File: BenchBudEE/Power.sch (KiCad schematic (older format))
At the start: 0 parts

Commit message: Power Protection and filtering module added
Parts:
- added C? (x2): C, ~, symbol C
- added F? (x4): FUSE, ~, symbol FUSE
- added L? (x2): INDUCTOR, ~, symbol INDUCTOR
- added P?: CONN_12X2, symbol CONN_12X2
- added R?: R, ~, symbol R
- added SW?: SWITCH_INV, ~, symbol SWITCH_INV
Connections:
- net labels added: +12P, +12V, +3.3V, +5V, -12P, -12V, GND
- wire segments 0 -> 39

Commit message: Fan/current module refactoring
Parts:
- removed F? (x4): FUSE, ~, symbol FUSE
- added TH? (x4): THERMISTOR, ~, symbol THERMISTOR
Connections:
- net labels added: +12C
- wire segments 39 -> 40
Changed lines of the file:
@@
 $Descr A4 11693 8268
 encoding utf-8
-Sheet 6 9
+Sheet 4 9
 Title ""
-Date "9 feb 2014"
+Date "11 feb 2014"
 Rev ""
 Comp ""
@@
 F 3 "" H 5000 1000 60  0000 C CNN
 	1    5000 1000
-	1    0    0    -1
-$EndComp
-$Comp
-L FUSE F?
-U 1 1 52F65207
-P 3800 1350
-F 0 "F?" H 3900 1400 40  0000 C CNN
-F 1 "FUSE" H 3700 1300 40  0000 C CNN
-F 2 "~" H 3800 1350 60  0000 C CNN
-F 3 "~" H 3800 1350 60  0000 C CNN
-	1    3800 1350
-	1    0    0    -1
-$EndComp
-$Comp
-L FUSE F?
-U 1 1 52F65214
-P 4550 1550
-F 0 "F?" H 4650 1600 40  0000 C CNN
-F 1 "FUSE" H 4450 1500 40  0000 C CNN
-F 2 "~" H 4550 1550 60  0000 C CNN
-F 3 "~" H 4550 1550 60  0000 C CNN
-	1    4550 1550
-	1    0    0    -1
-$EndComp
-$Comp
-L FUSE F?
-U 1 1 52F6521A
-P 5400 1750
-F 0 "F?" H 5500 1800 40  0000 C CNN
-F 1 "FUSE" H 5300 1700 40  0000 C CNN
-F 2 "~" H 5400 1750 60  0000 C CNN
-F 3 "~" H 5400 1750 60  0000 C CNN
-	1    5400 1750
-	1    0    0    -1
-$EndComp
-$Comp
-L FUSE F?
-U 1 1 52F65220
-P 6150 1950
-F 0 "F?" H 6250 2000 40  0000 C CNN
-F 1 "FUSE" H 6050 1900 40  0000 C CNN
-F 2 "~" H 6150 1950 60  0000 C CNN
-F 3 "~" H 6150 1950 60  0000 C CNN
-	1    6150 1950
 	1    0    0    -1
 $EndComp
@@
 	-1   0    0    1
 $EndComp
+Wire Wire Line
+	3400 1750 3400 1000
+Connection ~ 3400 1750
+$Comp
+L +12C #PWR?
+U 1 1 52FA733D
+P 3400 1000
+F 0 "#PWR?" H 3400 970 30  0001 C CNN
+F 1 "+12C" H 3400 1110 40  0000 C CNN
+F 2 "" H 3400 1000 60  0000 C CNN
+F 3 "" H 3400 1000 60  0000 C CNN
+	1    3400 1000
+	1    0    0    -1
+$EndComp
+$Comp
+L THERMISTOR TH?
+U 1 1 52FA7ACC
+P 3800 1350
+F 0 "TH?" V 3900 1400 50  0000 C CNN
+F 1 "THERMISTOR" V 3700 1350 50  0000 C CNN
+F 2 "~" H 3800 1350 60  0000 C CNN
+F 3 "~" H 3800 1350 60  0000 C CNN
+	1    3800 1350
+	0    -1   -1   0
+$EndComp
+$Comp
+L THERMISTOR TH?
+U 1 1 52FA7AD9
+P 4550 1550
+F 0 "TH?" V 4650 1600 50  0000 C CNN
+F 1 "THERMISTOR" V 4450 1550 50  0000 C CNN
+F 2 "~" H 4550 1550 60  0000 C CNN
+F 3 "~" H 4550 1550 60  0000 C CNN
+	1    4550 1550
+	0    -1   -1   0
+$EndComp
+$Comp
+L THERMISTOR TH?
+U 1 1 52FA7ADF
+P 5400 1750
+F 0 "TH?" V 5500 1800 50  0000 C CNN
+F 1 "THERMISTOR" V 5300 1750 50  0000 C CNN
+F 2 "~" H 5400 1750 60  0000 C CNN
+F 3 "~" H 5400 1750 60  0000 C CNN
+	1    5400 1750
+	0    -1   -1   0
+$EndComp
+$Comp
+L THERMISTOR TH?
+U 1 1 52FA7AE5
+P 6150 1950
+F 0 "TH?" V 6250 2000 50  0000 C CNN
+F 1 "THERMISTOR" V 6050 1950 50  0000 C CNN
+F 2 "~" H 6150 1950 60  0000 C CNN
+F 3 "~" H 6150 1950 60  0000 C CNN
+	1    6150 1950
+	0    -1   -1   0
+$EndComp
 $EndSCHEMATC

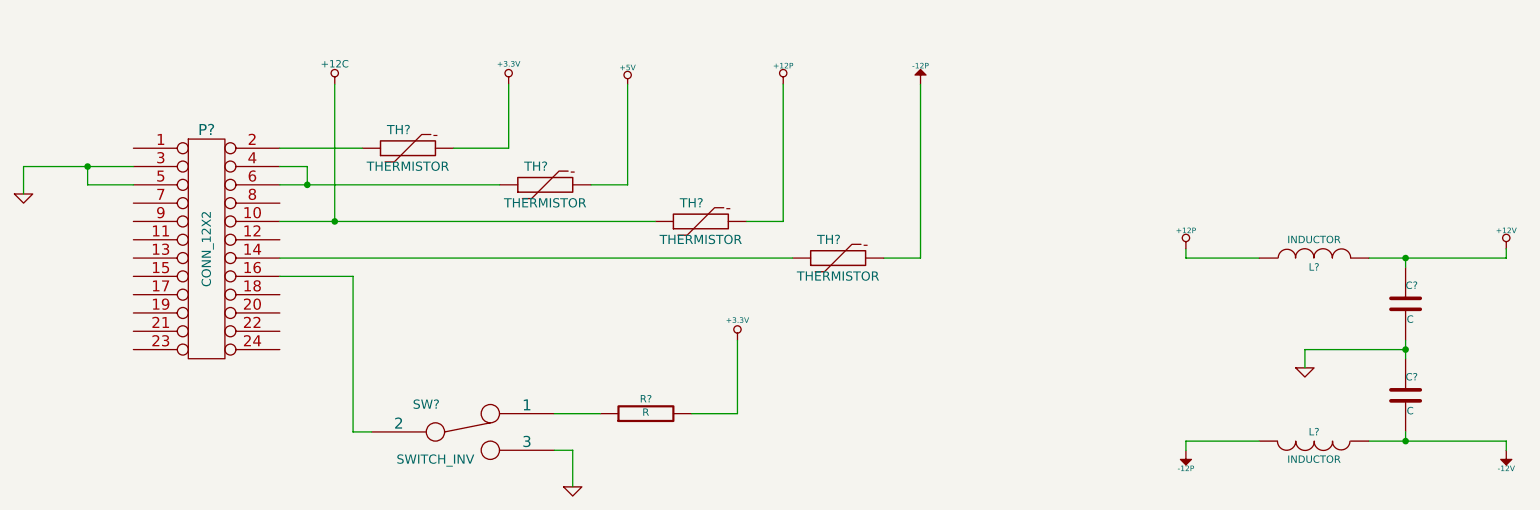
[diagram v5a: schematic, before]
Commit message: PCB Outline created and changes during  components choice
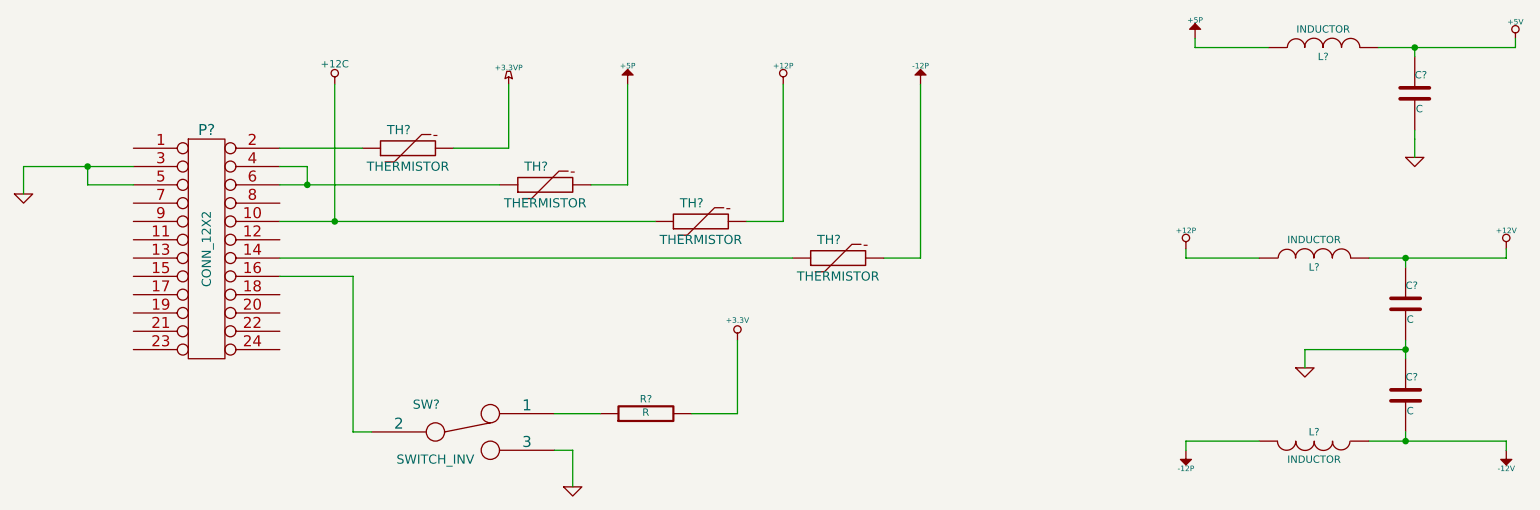
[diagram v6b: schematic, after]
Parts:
- added C?: C, ~, symbol C
- added L?: INDUCTOR, ~, symbol INDUCTOR
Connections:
- net +3.3V: no longer TH?.2
- net +5V: now also C?.1, L?.2; no longer TH?.2
- net GND: now also C?.2
- new net +3.3VP: TH?.2
- new net +5P: L?.1, TH?.2
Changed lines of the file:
@@
 Sheet 4 9
 Title ""
-Date "11 feb 2014"
+Date "16 feb 2014"
 Rev ""
 Comp ""
@@
 	1    0    0    -1
 $EndComp
-$Comp
-L +3.3V #PWR?
-U 1 1 52F651A0
-P 4350 1000
-F 0 "#PWR?" H 4350 960 30  0001 C CNN
-F 1 "+3.3V" H 4350 1110 30  0000 C CNN
-F 2 "" H 4350 1000 60  0000 C CNN
-F 3 "" H 4350 1000 60  0000 C CNN
-	1    4350 1000
-	1    0    0    -1
-$EndComp
-$Comp
-L +5V #PWR?
-U 1 1 52F651AF
-P 5000 1000
-F 0 "#PWR?" H 5000 1090 20  0001 C CNN
-F 1 "+5V" H 5000 1090 30  0000 C CNN
-F 2 "" H 5000 1000 60  0000 C CNN
-F 3 "" H 5000 1000 60  0000 C CNN
-	1    5000 1000
-	1    0    0    -1
-$EndComp
 Wire Wire Line
 	3100 1350 3550 1350
@@
 	3250 1450 3250 1550
 Wire Wire Line
-	3100 1550 4300 1550
+	3100 1550 3250 1550
+Wire Wire Line
+	3250 1550 4300 1550
 Connection ~ 3250 1550
 Wire Wire Line
@@
 	5000 1550 5000 1000
 Wire Wire Line
-	3100 1750 5150 1750
+	3100 1750 3400 1750
+Wire Wire Line
+	3400 1750 5150 1750
 Wire Wire Line
 	3100 1950 5900 1950
@@
 	6600 1950 6400 1950
 Wire Wire Line
-	1700 1450 2300 1450
+	1700 1450 2050 1450
+Wire Wire Line
+	2050 1450 2300 1450
 Wire Wire Line
 	2050 1550 2300 1550
@@
 	8050 2950 8450 2950
 Wire Wire Line
-	9050 2950 9800 2950
+	9050 2950 9250 2950
+Wire Wire Line
+	9250 2950 9800 2950
 Wire Wire Line
 	9250 2950 9250 2900
 Wire Wire Line
-	9250 2500 9250 2400
+	9250 2500 9250 2450
+Wire Wire Line
+	9250 2450 9250 2400
 Wire Wire Line
 	9250 2000 9250 1950
 Wire Wire Line
-	9050 1950 9800 1950
+	9050 1950 9250 1950
+Wire Wire Line
+	9250 1950 9800 1950
 Wire Wire Line
 	9250 2450 8700 2450
@@
 	0    -1   -1   0
 $EndComp
+$Comp
+L INDUCTOR L?
+U 1 1 5300ADAC
+P 8800 800
+F 0 "L?" V 8750 800 40  0000 C CNN
+F 1 "INDUCTOR" V 8900 800 40  0000 C CNN
+F 2 "~" H 8800 800 60  0000 C CNN
+F 3 "~" H 8800 800 60  0000 C CNN
+	1    8800 800
+	0    -1   -1   0
+$EndComp
+$Comp
+L C C?
+U 1 1 5300ADB2
+P 9300 1050
+F 0 "C?" H 9300 1150 40  0000 L CNN
+F 1 "C" H 9306 965 40  0000 L CNN
+F 2 "~" H 9338 900 30  0000 C CNN
+F 3 "~" H 9300 1050 60  0000 C CNN
+	1    9300 1050
+	1    0    0    -1
+$EndComp
+Wire Wire Line
+	8500 800  8100 800
+Wire Wire Line
+	8100 800  8100 750
+Wire Wire Line
+	9300 850  9300 800
+Wire Wire Line
+	9100 800  9300 800
+Wire Wire Line
+	9300 800  9850 800
+Wire Wire Line
+	9300 1300 9300 1300
+Wire Wire Line
+	9300 1300 9300 1400
+$Comp
+L GND #PWR?
+U 1 1 5300ADC6
+P 9300 1400
+F 0 "#PWR?" H 9300 1400 30  0001 C CNN
+F 1 "GND" H 9300 1330 30  0001 C CNN
+F 2 "" H 9300 1400 60  0000 C CNN
+F 3 "" H 9300 1400 60  0000 C CNN
+	1    9300 1400
+	1    0    0    -1
+$EndComp
+Wire Wire Line
+	9850 800  9850 750
+Connection ~ 9300 800
+Wire Wire Line
+	9300 1250 9300 1300
+$Comp
+L +5P #PWR?
+U 1 1 5300AE45
+P 5000 1000
+F 0 "#PWR?" H 5000 1130 20  0001 C CNN
+F 1 "+5P" H 5000 1100 30  0000 C CNN
+F 2 "" H 5000 1000 60  0000 C CNN
+F 3 "" H 5000 1000 60  0000 C CNN
+	1    5000 1000
+	1    0    0    -1
+$EndComp
+$Comp
+L +3.3VP #PWR?
+U 1 1 5300AE54
+P 4350 1000
+F 0 "#PWR?" H 4400 1030 20  0001 C CNN
+F 1 "+3.3VP" H 4350 1090 30  0000 C CNN
+F 2 "" H 4350 1000 60  0000 C CNN
+F 3 "" H 4350 1000 60  0000 C CNN
+	1    4350 1000
+	1    0    0    -1
+$EndComp
+$Comp
+L +5P #PWR?
+U 1 1 5300AE61
+P 8100 750
+F 0 "#PWR?" H 8100 880 20  0001 C CNN
+F 1 "+5P" H 8100 850 30  0000 C CNN
+F 2 "" H 8100 750 60  0000 C CNN
+F 3 "" H 8100 750 60  0000 C CNN
+	1    8100 750
+	1    0    0    -1
+$EndComp
+$Comp
+L +5V #PWR?
+U 1 1 5300AE69
+P 9850 750
+F 0 "#PWR?" H 9850 840 20  0001 C CNN
+F 1 "+5V" H 9850 840 30  0000 C CNN
+F 2 "" H 9850 750 60  0000 C CNN
+F 3 "" H 9850 750 60  0000 C CNN
+	1    9850 750
+	1    0    0    -1
+$EndComp
 $EndSCHEMATC

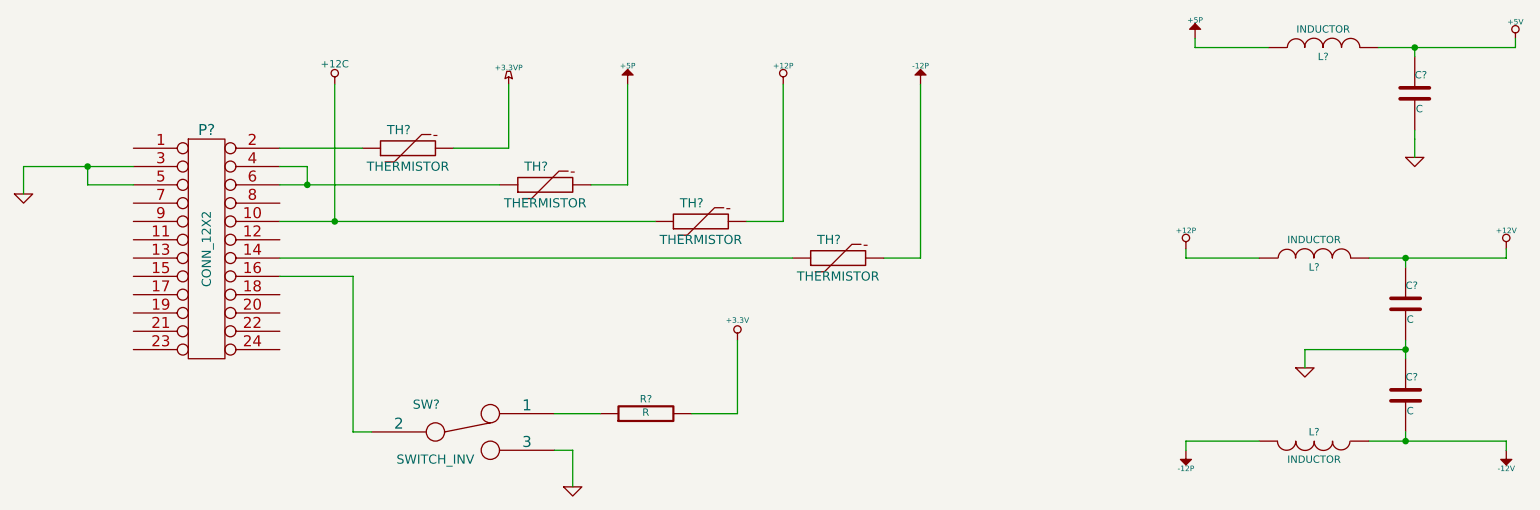
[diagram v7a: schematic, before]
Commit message: Associating and Placing the Relay Module
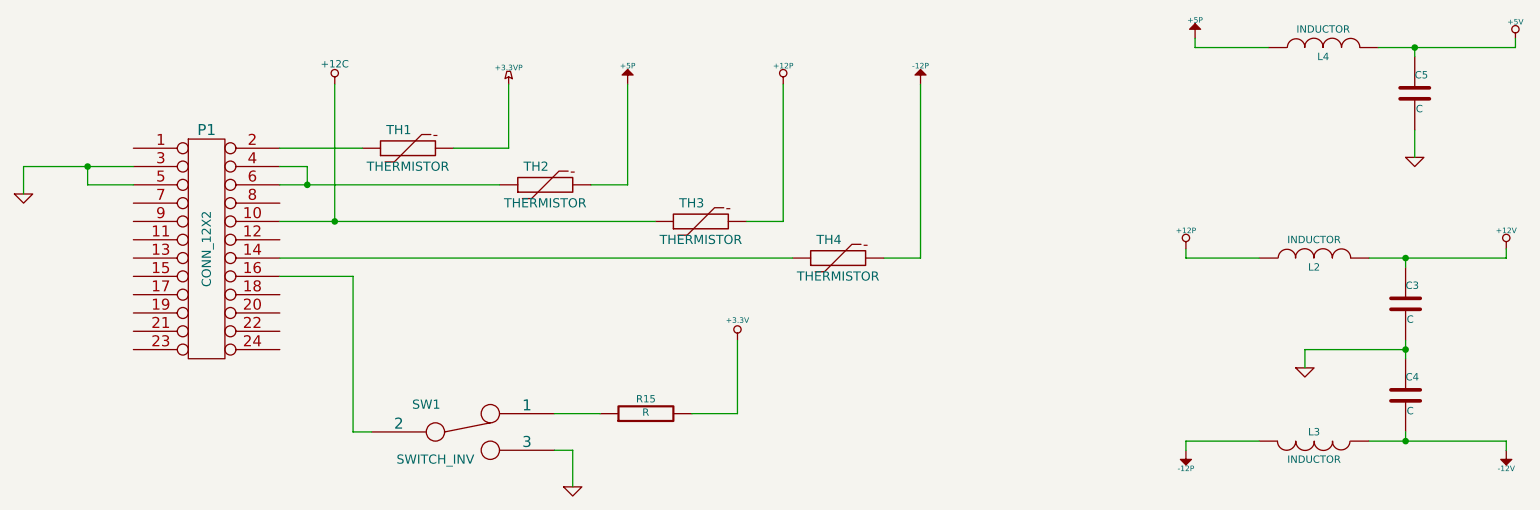
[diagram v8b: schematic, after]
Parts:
- gave numbers to parts that had none: 13
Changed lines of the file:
@@
 $EndDescr
 $Comp
-L CONN_12X2 P?
+L CONN_12X2 P1
 U 1 1 52F6517B
 P 2700 1900
-F 0 "P?" H 2700 2550 60  0000 C CNN
+F 0 "P1" H 2700 2550 60  0000 C CNN
 F 1 "CONN_12X2" V 2700 1900 50  0000 C CNN
 F 2 "" H 2700 1900 60  0000 C CNN
@@
 	1700 1450 1700 1600
 $Comp
-L GND #PWR015
+L GND #PWR15
 U 1 1 52F65191
 P 1700 1600
-F 0 "#PWR015" H 1700 1600 30  0001 C CNN
+F 0 "#PWR15" H 1700 1600 30  0001 C CNN
 F 1 "GND" H 1700 1530 30  0001 C CNN
 F 2 "" H 1700 1600 60  0000 C CNN
@@
 	3250 1450 3250 1550
 Wire Wire Line
-	3100 1550 3250 1550
-Wire Wire Line
-	3250 1550 4300 1550
+	3100 1550 4300 1550
 Connection ~ 3250 1550
 Wire Wire Line
@@
 	5000 1550 5000 1000
 Wire Wire Line
-	3100 1750 3400 1750
-Wire Wire Line
-	3400 1750 5150 1750
+	3100 1750 5150 1750
 Wire Wire Line
 	3100 1950 5900 1950
 $Comp
-L +12P #PWR016
+L +12P #PWR21
 U 1 1 52F65291
 P 5850 1000
-F 0 "#PWR016" H 5850 970 30  0001 C CNN
+F 0 "#PWR21" H 5850 970 30  0001 C CNN
 F 1 "+12P" H 5850 1100 30  0000 C CNN
 F 2 "" H 5850 1000 60  0000 C CNN
@@
 	5850 1750 5650 1750
 $Comp
-L -12P #PWR017
+L -12P #PWR22
 U 1 1 52F65D56
 P 6600 1000
-F 0 "#PWR017" H 6600 1130 20  0001 C CNN
+F 0 "#PWR22" H 6600 1130 20  0001 C CNN
 F 1 "-12P" H 6600 1100 30  0000 C CNN
 F 2 "" H 6600 1000 60  0000 C CNN
@@
 	6600 1950 6400 1950
 Wire Wire Line
-	1700 1450 2050 1450
-Wire Wire Line
-	2050 1450 2300 1450
+	1700 1450 2300 1450
 Wire Wire Line
 	2050 1550 2300 1550
@@
 Connection ~ 2050 1450
 $Comp
-L SWITCH_INV SW?
+L SWITCH_INV SW1
 U 1 1 52F65DFE
 P 4100 2900
-F 0 "SW?" H 3900 3050 50  0000 C CNN
+F 0 "SW1" H 3900 3050 50  0000 C CNN
 F 1 "SWITCH_INV" H 3950 2750 50  0000 C CNN
 F 2 "~" H 4100 2900 60  0000 C CNN
@@
 $EndComp
 $Comp
-L GND #PWR018
+L GND #PWR18
 U 1 1 52F65E0B
 P 4700 3200
-F 0 "#PWR018" H 4700 3200 30  0001 C CNN
+F 0 "#PWR18" H 4700 3200 30  0001 C CNN
 F 1 "GND" H 4700 3130 30  0001 C CNN
 F 2 "" H 4700 3200 60  0000 C CNN
@@
 	3500 2900 3600 2900
 $Comp
-L R R?
+L R R15
 U 1 1 52F66000
 P 5100 2800
-F 0 "R?" V 5180 2800 40  0000 C CNN
+F 0 "R15" V 5180 2800 40  0000 C CNN
 F 1 "R" V 5107 2801 40  0000 C CNN
 F 2 "~" V 5030 2800 30  0000 C CNN
@@
 	5600 2800 5600 2400
 $Comp
-L +3.3V #PWR019
+L +3.3V #PWR20
 U 1 1 52F66046
 P 5600 2400
-F 0 "#PWR019" H 5600 2360 30  0001 C CNN
+F 0 "#PWR20" H 5600 2360 30  0001 C CNN
 F 1 "+3.3V" H 5600 2510 30  0000 C CNN
 F 2 "" H 5600 2400 60  0000 C CNN
@@
 $EndComp
 $Comp
-L -12P #PWR020
+L -12P #PWR24
 U 1 1 52F6604C
 P 8050 3000
-F 0 "#PWR020" H 8050 3130 20  0001 C CNN
+F 0 "#PWR24" H 8050 3130 20  0001 C CNN
 F 1 "-12P" H 8050 3100 30  0000 C CNN
 F 2 "" H 8050 3000 60  0000 C CNN
@@
 $EndComp
 $Comp
-L +12P #PWR021
+L +12P #PWR23
 U 1 1 52F66052
 P 8050 1900
-F 0 "#PWR021" H 8050 1870 30  0001 C CNN
+F 0 "#PWR23" H 8050 1870 30  0001 C CNN
 F 1 "+12P" H 8050 2000 30  0000 C CNN
 F 2 "" H 8050 1900 60  0000 C CNN
@@
 $EndComp
 $Comp
-L INDUCTOR L?
+L INDUCTOR L2
 U 1 1 52F6605A
 P 8750 1950
-F 0 "L?" V 8700 1950 40  0000 C CNN
+F 0 "L2" V 8700 1950 40  0000 C CNN
 F 1 "INDUCTOR" V 8850 1950 40  0000 C CNN
 F 2 "~" H 8750 1950 60  0000 C CNN
@@
 $EndComp
 $Comp
-L INDUCTOR L?
+L INDUCTOR L3
 U 1 1 52F66067
 P 8750 2950
-F 0 "L?" V 8700 2950 40  0000 C CNN
+F 0 "L3" V 8700 2950 40  0000 C CNN
 F 1 "INDUCTOR" V 8850 2950 40  0000 C CNN
 F 2 "~" H 8750 2950 60  0000 C CNN
@@
 $EndComp
 $Comp
-L C C?
+L C C3
 U 1 1 52F6606F
 P 9250 2200
-F 0 "C?" H 9250 2300 40  0000 L CNN
+F 0 "C3" H 9250 2300 40  0000 L CNN
 F 1 "C" H 9256 2115 40  0000 L CNN
 F 2 "~" H 9288 2050 30  0000 C CNN
@@
 $EndComp
 $Comp
-L C C?
+L C C4
 U 1 1 52F6607C
 P 9250 2700
-F 0 "C?" H 9250 2800 40  0000 L CNN
+F 0 "C4" H 9250 2800 40  0000 L CNN
 F 1 "C" H 9256 2615 40  0000 L CNN
 F 2 "~" H 9288 2550 30  0000 C CNN
@@
 	8050 2950 8450 2950
 Wire Wire Line
-	9050 2950 9250 2950
-Wire Wire Line
-	9250 2950 9800 2950
+	9050 2950 9800 2950
 Wire Wire Line
 	9250 2950 9250 2900
 Wire Wire Line
-	9250 2500 9250 2450
-Wire Wire Line
-	9250 2450 9250 2400
+	9250 2400 9250 2500
 Wire Wire Line
 	9250 2000 9250 1950
 Wire Wire Line
-	9050 1950 9250 1950
-Wire Wire Line
-	9250 1950 9800 1950
+	9050 1950 9800 1950
 Wire Wire Line
 	9250 2450 8700 2450
@@
 Connection ~ 9250 2450
 $Comp
-L GND #PWR022
+L GND #PWR26
 U 1 1 52F6614F
 P 8700 2550
-F 0 "#PWR022" H 8700 2550 30  0001 C CNN
+F 0 "#PWR26" H 8700 2550 30  0001 C CNN
 F 1 "GND" H 8700 2480 30  0001 C CNN
 F 2 "" H 8700 2550 60  0000 C CNN
@@
 Connection ~ 9250 1950
 $Comp
-L +12V #PWR023
+L +12V #PWR28
 U 1 1 52F661D8
 P 9800 1900
-F 0 "#PWR023" H 9800 1850 20  0001 C CNN
+F 0 "#PWR28" H 9800 1850 20  0001 C CNN
 F 1 "+12V" H 9800 2000 30  0000 C CNN
 F 2 "" H 9800 1900 60  0000 C CNN
@@
 $EndComp
 $Comp
-L -12V #PWR024
+L -12V #PWR29
 U 1 1 52F661F1
 P 9800 3000
-F 0 "#PWR024" H 9800 3130 20  0001 C CNN
+F 0 "#PWR29" H 9800 3130 20  0001 C CNN
 F 1 "-12V" H 9800 3100 30  0000 C CNN
 F 2 "" H 9800 3000 60  0000 C CNN
@@
 Connection ~ 3400 1750
 $Comp
-L +12C #PWR025
+L +12C #PWR16
 U 1 1 52FA733D
 P 3400 1000
-F 0 "#PWR025" H 3400 970 30  0001 C CNN
+F 0 "#PWR16" H 3400 970 30  0001 C CNN
 F 1 "+12C" H 3400 1110 40  0000 C CNN
 F 2 "" H 3400 1000 60  0000 C CNN
@@
 $EndComp
 $Comp
-L THERMISTOR TH?
+L THERMISTOR TH1
 U 1 1 52FA7ACC
 P 3800 1350
-F 0 "TH?" V 3900 1400 50  0000 C CNN
+F 0 "TH1" V 3900 1400 50  0000 C CNN
 F 1 "THERMISTOR" V 3700 1350 50  0000 C CNN
 F 2 "~" H 3800 1350 60  0000 C CNN
@@
 $EndComp
 $Comp
-L THERMISTOR TH?
+L THERMISTOR TH2
 U 1 1 52FA7AD9
 P 4550 1550
-F 0 "TH?" V 4650 1600 50  0000 C CNN
+F 0 "TH2" V 4650 1600 50  0000 C CNN
 F 1 "THERMISTOR" V 4450 1550 50  0000 C CNN
 F 2 "~" H 4550 1550 60  0000 C CNN
@@
 $EndComp
 $Comp
-L THERMISTOR TH?
+L THERMISTOR TH3
 U 1 1 52FA7ADF
 P 5400 1750
-F 0 "TH?" V 5500 1800 50  0000 C CNN
+F 0 "TH3" V 5500 1800 50  0000 C CNN
 F 1 "THERMISTOR" V 5300 1750 50  0000 C CNN
 F 2 "~" H 5400 1750 60  0000 C CNN
@@
 $EndComp
 $Comp
-L THERMISTOR TH?
+L THERMISTOR TH4
 U 1 1 52FA7AE5
 P 6150 1950
-F 0 "TH?" V 6250 2000 50  0000 C CNN
+F 0 "TH4" V 6250 2000 50  0000 C CNN
 F 1 "THERMISTOR" V 6050 1950 50  0000 C CNN
 F 2 "~" H 6150 1950 60  0000 C CNN
@@
 $EndComp
 $Comp
-L INDUCTOR L?
+L INDUCTOR L4
 U 1 1 5300ADAC
 P 8800 800
-F 0 "L?" V 8750 800 40  0000 C CNN
+F 0 "L4" V 8750 800 40  0000 C CNN
 F 1 "INDUCTOR" V 8900 800 40  0000 C CNN
 F 2 "~" H 8800 800 60  0000 C CNN
@@
 $EndComp
 $Comp
-L C C?
+L C C5
 U 1 1 5300ADB2
 P 9300 1050
-F 0 "C?" H 9300 1150 40  0000 L CNN
+F 0 "C5" H 9300 1150 40  0000 L CNN
 F 1 "C" H 9306 965 40  0000 L CNN
 F 2 "~" H 9338 900 30  0000 C CNN
@@
 	9300 850  9300 800
 Wire Wire Line
-	9100 800  9300 800
-Wire Wire Line
-	9300 800  9850 800
+	9100 800  9850 800
 Wire Wire Line
 	9300 1300 9300 1300
 Wire Wire Line
-	9300 1300 9300 1400
-$Comp
-L GND #PWR026
+	9300 1250 9300 1400
+$Comp
+L GND #PWR27
 U 1 1 5300ADC6
 P 9300 1400
-F 0 "#PWR026" H 9300 1400 30  0001 C CNN
+F 0 "#PWR27" H 9300 1400 30  0001 C CNN
 F 1 "GND" H 9300 1330 30  0001 C CNN
 F 2 "" H 9300 1400 60  0000 C CNN
@@
 	9850 800  9850 750
 Connection ~ 9300 800
-Wire Wire Line
-	9300 1250 9300 1300
-$Comp
-L +5P #PWR?
+$Comp
+L +5P #PWR19
 U 1 1 5300AE45
 P 5000 1000
-F 0 "#PWR?" H 5000 1130 20  0001 C CNN
+F 0 "#PWR19" H 5000 1130 20  0001 C CNN
 F 1 "+5P" H 5000 1100 30  0000 C CNN
 F 2 "" H 5000 1000 60  0000 C CNN
@@
 $EndComp
 $Comp
-L +3.3VP #PWR027
+L +3.3VP #PWR17
 U 1 1 5300AE54
 P 4350 1000
-F 0 "#PWR027" H 4400 1030 20  0001 C CNN
+F 0 "#PWR17" H 4400 1030 20  0001 C CNN
 F 1 "+3.3VP" H 4350 1090 30  0000 C CNN
 F 2 "" H 4350 1000 60  0000 C CNN
@@
 $EndComp
 $Comp
-L +5P #PWR?
+L +5P #PWR25
 U 1 1 5300AE61
 P 8100 750
-F 0 "#PWR?" H 8100 880 20  0001 C CNN
+F 0 "#PWR25" H 8100 880 20  0001 C CNN
 F 1 "+5P" H 8100 850 30  0000 C CNN
 F 2 "" H 8100 750 60  0000 C CNN
@@
 $EndComp
 $Comp
-L +5V #PWR028
+L +5V #PWR30
 U 1 1 5300AE69
 P 9850 750
-F 0 "#PWR028" H 9850 840 20  0001 C CNN
+F 0 "#PWR30" H 9850 840 20  0001 C CNN
 F 1 "+5V" H 9850 840 30  0000 C CNN
 F 2 "" H 9850 750 60  0000 C CNN
